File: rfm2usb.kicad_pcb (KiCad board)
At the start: 4 copper layers, 53 x 21 mm, 23 parts, among them J1 USB_B_Micro, J2 DBG, J4 Conn_Coaxial, J5 UART, U1 AP2210N-3.3TRG1, U2 STM32F042K6Tx, U3 RFM69HCW, Y1 8MHz

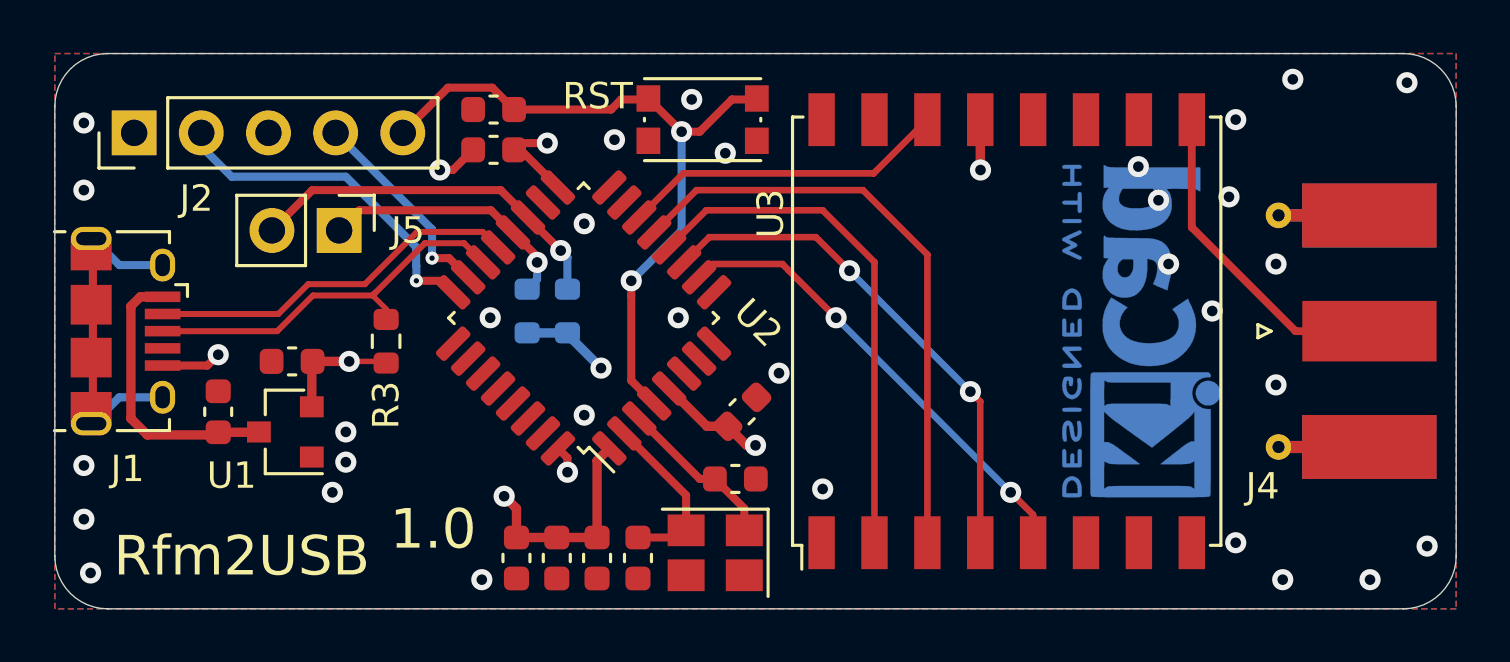
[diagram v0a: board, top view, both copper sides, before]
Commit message: change stm32 footprint
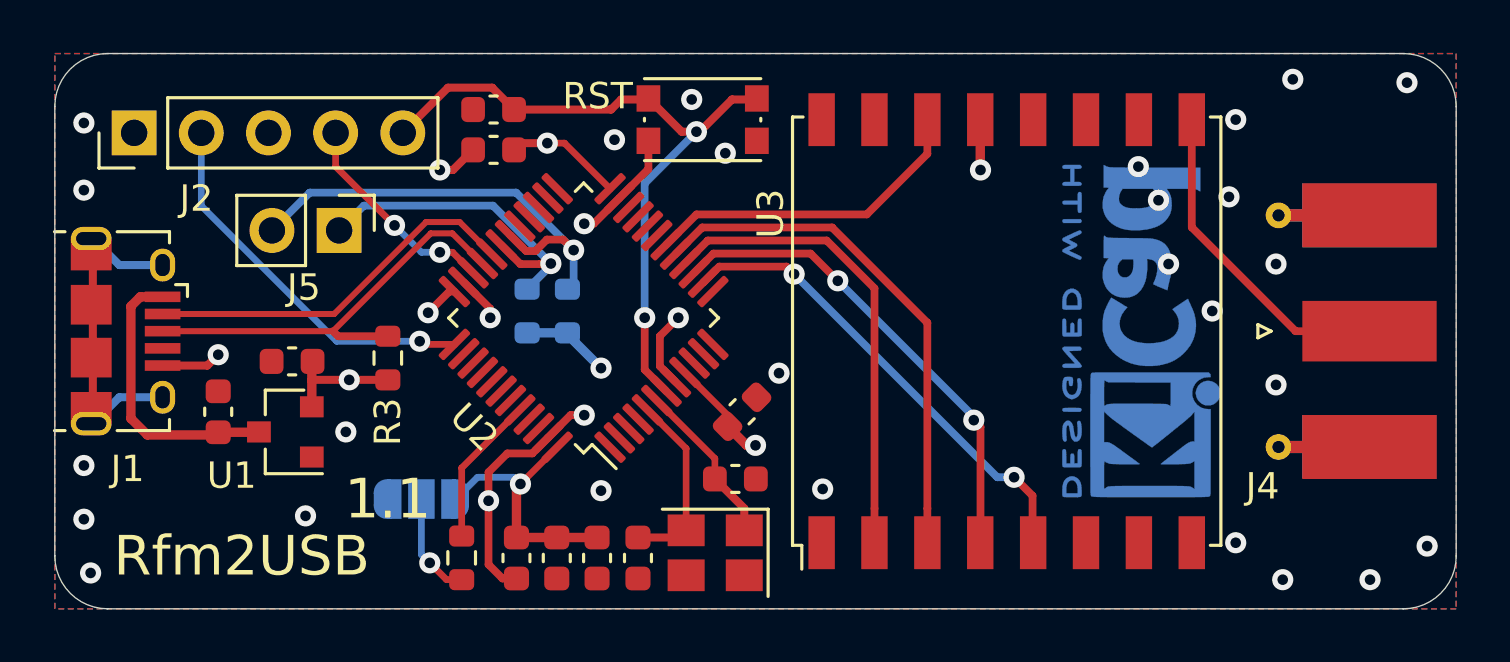
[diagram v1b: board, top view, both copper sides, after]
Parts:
- added JP1: BOOT0, Jumper:SolderJumper-3_P1.3mm_Open_RoundedPad1.0x1.5mm_NumberLabels, B.Cu at (113.9, 96.8)
- added R4: 10k, Resistor_SMD:R_0603_1608Metric, F.Cu at (115.4, 99.1)
- J4: value Conn_Coaxial -> SMA
- U2: value STM32F042K6Tx -> STM32L151CBT; footprint Package_QFP:LQFP-32_7x7mm_P0.8mm -> Package_QFP:LQFP-48_7x7mm_P0.5mm
- moved R3 0.64 mm to (112.6, 91.5)
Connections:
- U2 pad 1: +3V3 -> Net-(U2-Pad1)
- U2 pad 10: ~SPI_SS -> Net-(U2-Pad10)
- U2 pad 11: SPI_CLK -> Net-(U2-Pad11)
- U2 pad 12: SPI_MISO -> Net-(U2-Pad12)
- U2 pad 13: SPI_MOSI -> Net-(U2-Pad13)
- U2 pad 14: ~RFM_IRQ -> ~SPI_SS
- U2 pad 15: Net-(U2-Pad15) -> SPI_CLK
- U2 pad 16: GND -> SPI_MISO
- U2 pad 17: +3V3 -> SPI_MOSI
- U2 pad 18: Net-(U2-Pad18) -> ~RFM_IRQ
- U2 pad 19: USART1_TX -> Net-(U2-Pad19)
- U2 pad 2: Net-(C9-Pad1) -> Net-(U2-Pad2)
- U2 pad 20: USART1_RX -> Net-(U2-Pad20)
- U2 pad 21: USB_D- -> Net-(U2-Pad21)
- U2 pad 22: USB_D+ -> Net-(U2-Pad22)
- U2 pad 23: SWDIO -> GND
- U2 pad 24: SWCLK -> +3V3
- U2 pad 3: Net-(C10-Pad1) -> Net-(U2-Pad3)
- U2 pad 30: Net-(U2-Pad30) -> USART1_TX
- U2 pad 31: Net-(U2-Pad31) -> USART1_RX
- U2 pad 32: GND -> USB_D-
- U2 pad 4: ~RESET -> Net-(U2-Pad4)
- U2 pad 5: +3V3 -> Net-(C9-Pad1)
- U2 pad 6: Net-(U2-Pad6) -> Net-(C10-Pad1)
- U2 pad 7: Net-(U2-Pad7) -> ~RESET
- U2 pad 8: Net-(U2-Pad8) -> GND
- U2 pad 9: Net-(U2-Pad9) -> +3V3
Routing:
- net GND: track 4.83 -> 22.1 mm, vias 35 -> 34
- net BOOT0: track 0.00 -> 5.68 mm
- net Net-(JP1-Pad2): track 0.00 -> 4.01 mm, vias 0 -> 1
- net +3V3: track 26.0 -> 29.7 mm, vias 6 -> 7
- net USART1_TX: track 14.1 -> 17.5 mm
- net SPI_MOSI: track 22.9 -> 19.8 mm
- net USART1_RX: track 9.92 -> 12.8 mm
- net SPI_MISO: track 19.8 -> 17.9 mm
- net SWCLK: track 13.1 -> 14.5 mm
- net USB_D+: track 14.9 -> 16.3 mm
- net SPI_CLK: track 19.5 -> 18.3 mm
- net Net-(C9-Pad1): track 6.57 -> 7.10 mm
- net SWDIO: track 7.91 -> 8.14 mm, vias 1 -> 2
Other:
- board text added: "1.1"
- board text removed: "1.0"

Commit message: fix clearance false pos
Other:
- net class 3.3V: clearance 0.2 -> 0.199999
- net class Default: clearance 0.2 -> 0.199999
- net class RF: clearance 0.2 -> 0.199999
- net class USB_DIFF: clearance 0.2 -> 0.199999
- rule trace_clearance: 0.2 -> 0.199999

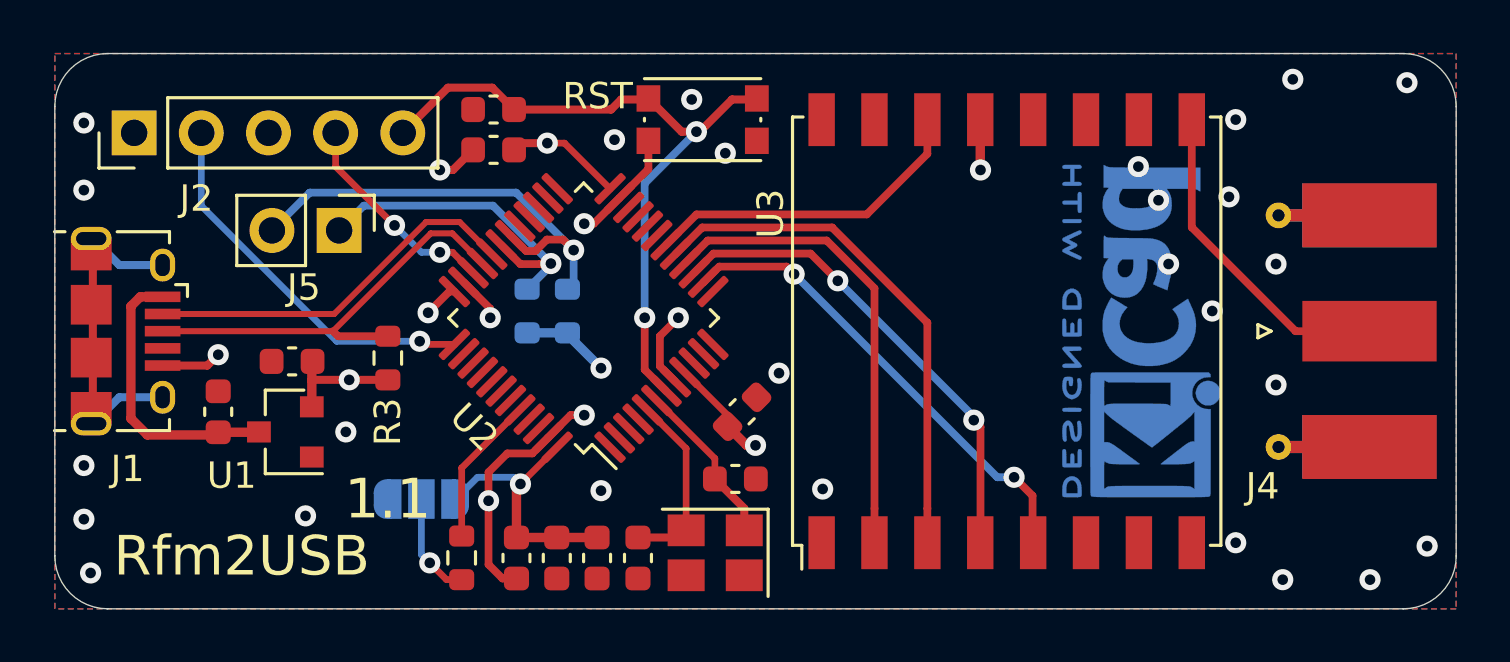
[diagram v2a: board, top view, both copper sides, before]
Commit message: replace reset button with boot button this is more useful
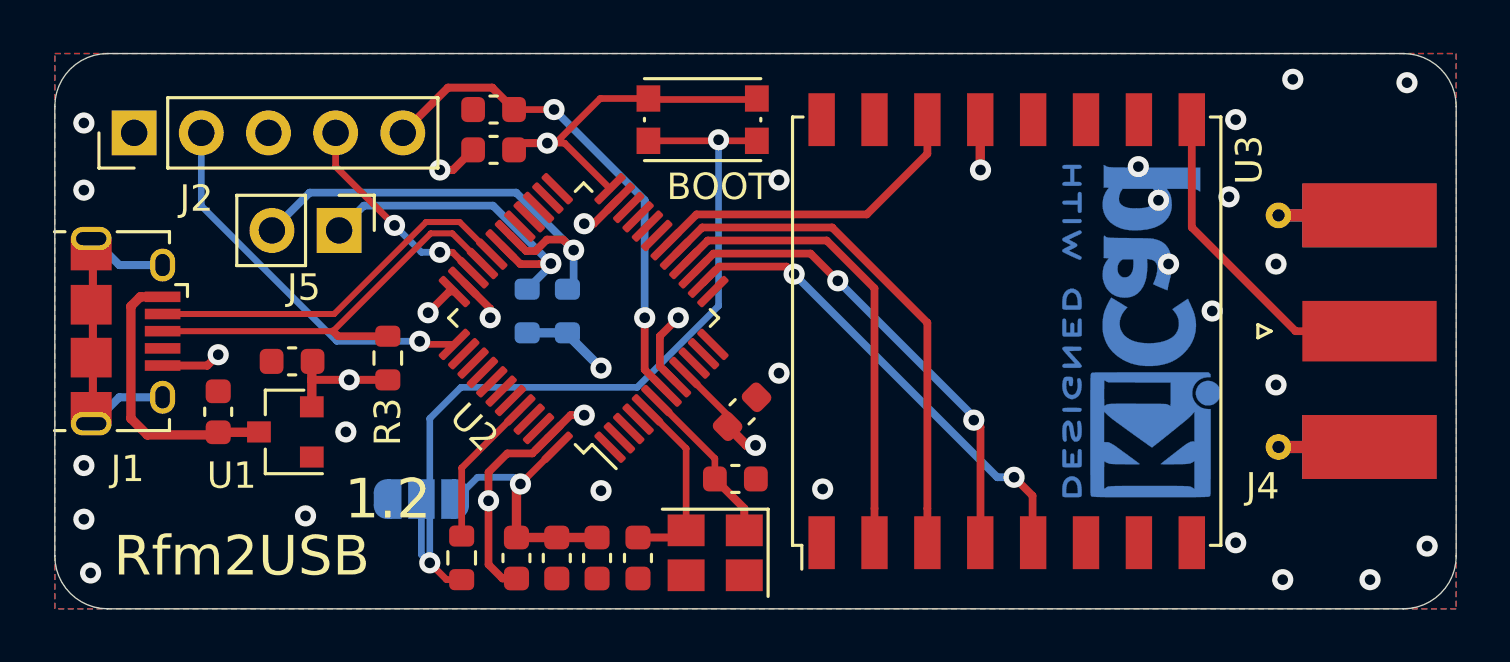
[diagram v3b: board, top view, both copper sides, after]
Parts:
- BOOT1: renamed from RST1; value RST -> BOOT
- JP1: value BOOT0 -> SolderJumper_3_Open
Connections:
- BOOT1 pad 1: GND -> Net-(BOOT1-Pad1)
- BOOT1 pad 2: ~RESET -> +3V3
- JP1 pad 2: Net-(JP1-Pad2) -> Net-(BOOT1-Pad1)
- R4 pad 1: Net-(JP1-Pad2) -> Net-(BOOT1-Pad1)
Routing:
- net Net-(BOOT1-Pad1): track 0.00 -> 32.6 mm, vias 0 -> 2
- net +3V3: track 29.7 -> 38.4 mm
- net ~RESET: track 26.6 -> 19.2 mm
- net Net-(JP1-Pad2): track 4.01 -> 0.00 mm, vias 1 -> 0
- net GND: track 22.1 -> 19.5 mm, vias 34 -> 32
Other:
- board text added: "1.2"
- board text removed: "1.1"
